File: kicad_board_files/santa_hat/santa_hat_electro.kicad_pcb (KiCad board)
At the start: 2 copper layers, 23.3 x 29.9 mm, 5 parts, among them U1 ELECTRO_HAT

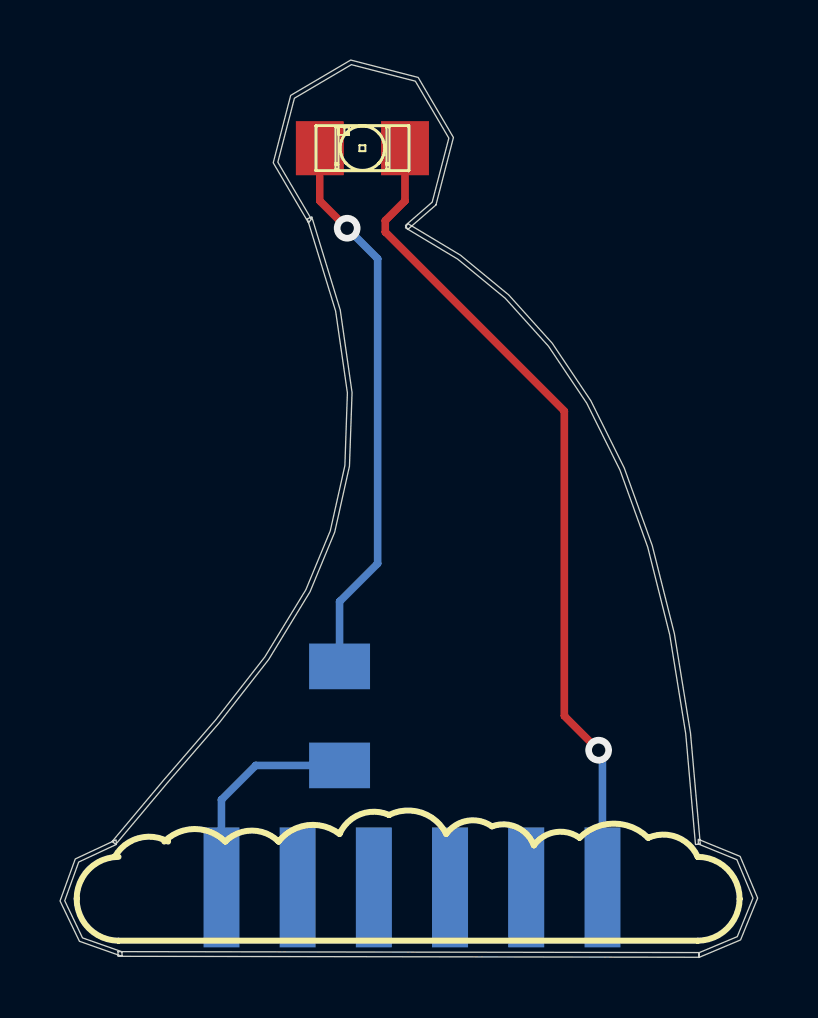
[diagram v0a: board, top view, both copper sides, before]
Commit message: fliped the header to the currect way
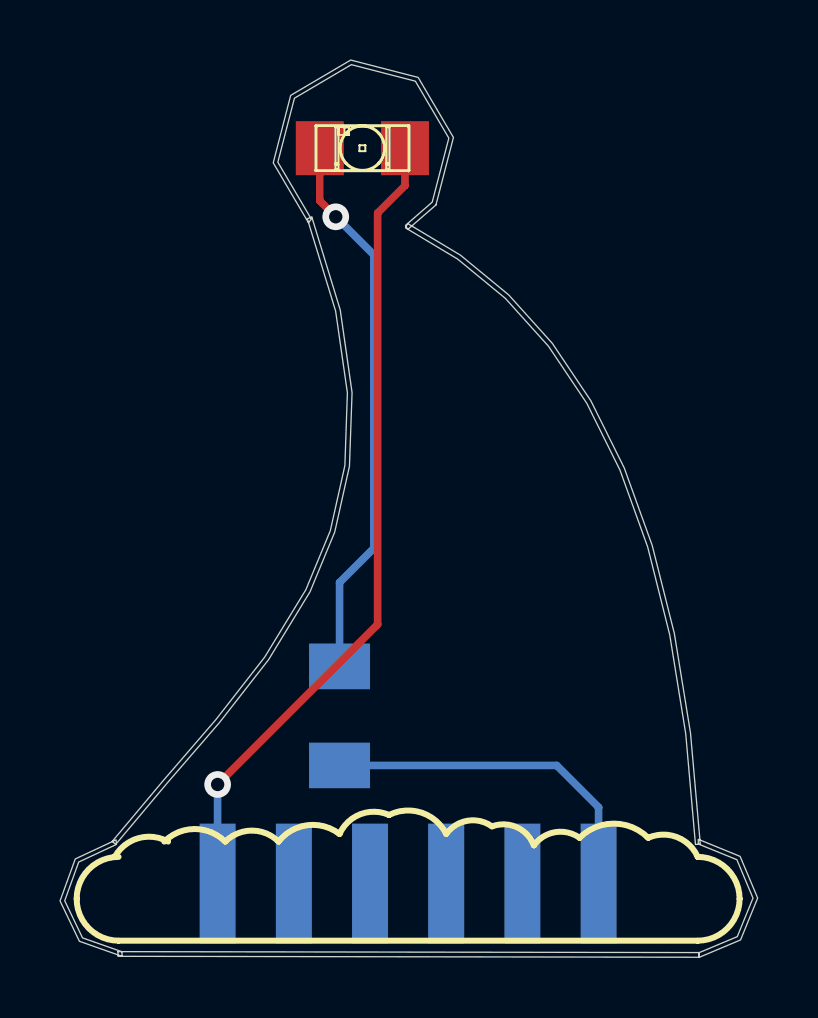
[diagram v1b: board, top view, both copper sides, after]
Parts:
- U1: footprint electro_hat_male_custom -> electro_hat_male_mirrored
- moved U1 0.18 mm to (199.4, 141.6)
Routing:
- net N-000005: track 7.33 -> 11.8 mm
- net N-000007: track 27.9 -> 27.1 mm
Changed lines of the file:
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@@
     (links 3)
     (no_connects 0)
-    (area 187.531625 109.510164 216.1159 148.299836)
+    (area 0 0 0 0)
     (thickness 1.6)
     (drawings 18)
-    (tracks 19)
+    (tracks 16)
     (zones 0)
     (modules 5)
@@
       (scale (xyz 0.17 0.16 0.16))
       (rotate (xyz 0 0 0))
-    )
-  )
-  (module electro_hat_male_custom (layer B.Cu)
-    (at 199.517 141.732)
-    (fp_text reference U1 (at 0 4.445) (layer B.SilkS) hide
-      (effects (font (size 1 1) (thickness 0.15)) (justify mirror))
-    )
-    (fp_text value ELECTRO_HAT (at 0 -4.953) (layer B.SilkS) hide
-      (effects (font (size 1 1) (thickness 0.15)) (justify mirror))
-    )
-    (pad 3 smd rect (at -1.27 0) (size 1.2 4)
-      (layers B.Cu B.Paste B.Mask)
-    )
-    (pad 4 smd rect (at 1.27 0) (size 1.2 4)
-      (layers B.Cu B.Paste B.Mask)
-    )
-    (pad 2 smd rect (at -3.81 0) (size 1.2 4)
-      (layers B.Cu B.Paste B.Mask)
-    )
-    (pad 1 smd rect (at -6.35 0) (size 1.2 4)
-      (layers B.Cu B.Paste B.Mask)
-      (net 1 N-000005)
-    )
-    (pad 5 smd rect (at 3.81 0) (size 1.2 4)
-      (layers B.Cu B.Paste B.Mask)
-    )
-    (pad 6 smd rect (at 6.35 0) (size 1.2 4)
-      (layers B.Cu B.Paste B.Mask)
-      (net 3 N-000007)
     )
   )
@@
       (xy -3.50012 3.50012) (xy -3.50012 3.50012)) (layer B.SilkS) (width 0.00254))
   )
+  (module electro_hat_male_mirrored (layer B.Cu)
+    (at 199.39 141.605)
+    (fp_text reference U1 (at 0 4.445) (layer B.SilkS)
+      (effects (font (size 1 1) (thickness 0.15)) (justify mirror))
+    )
+    (fp_text value ELECTRO_HAT (at 0 -4.953) (layer B.SilkS)
+      (effects (font (size 1 1) (thickness 0.15)) (justify mirror))
+    )
+    (pad 3 smd rect (at 1.27 0) (size 1.2 4)
+      (layers B.Cu B.Paste B.Mask)
+    )
+    (pad 4 smd rect (at -1.27 0) (size 1.2 4)
+      (layers B.Cu B.Paste B.Mask)
+    )
+    (pad 2 smd rect (at 3.81 0) (size 1.2 4)
+      (layers B.Cu B.Paste B.Mask)
+    )
+    (pad 1 smd rect (at 6.35 0) (size 1.2 4)
+      (layers B.Cu B.Paste B.Mask)
+      (net 1 N-000005)
+    )
+    (pad 5 smd rect (at -3.81 0) (size 1.2 4)
+      (layers B.Cu B.Paste B.Mask)
+    )
+    (pad 6 smd rect (at -6.35 0) (size 1.2 4)
+      (layers B.Cu B.Paste B.Mask)
+      (net 3 N-000007)
+    )
+  )
   (gr_text 2016 (at 201.93 128.905) (layer B.SilkS)
     (effects (font (size 1 1) (thickness 0.25)) (justify mirror))
@@
   (gr_arc (start 209.042 142.113) (end 210.439 142.113) (angle 90) (layer F.SilkS) (width 0.2))
   (gr_arc (start 209.042 142.113) (end 209.042 140.716) (angle 90) (layer F.SilkS) (width 0.2))
-  (segment (start 193.167 141.732) (end 193.167 138.811) (width 0.254) (layer B.Cu) (net 1))
-  (segment (start 194.31 137.668) (end 197.104 137.668) (width 0.254) (layer B.Cu) (net 1))
-  (segment (start 193.167 138.811) (end 194.31 137.668) (width 0.254) (layer B.Cu) (net 1))
-  (segment (start 197.104 134.366) (end 197.104 132.207) (width 0.254) (layer B.Cu) (net 2))
-  (segment (start 196.44614 118.84914) (end 196.44614 117.094) (width 0.254) (layer F.Cu) (net 2))
-  (segment (start 197.358 119.761) (end 196.44614 118.84914) (width 0.254) (layer F.Cu) (net 2))
-  (via (at 197.358 119.761) (size 0.889) (layers F.Cu B.Cu) (net 2))
-  (segment (start 198.374 120.777) (end 197.358 119.761) (width 0.254) (layer B.Cu) (net 2))
-  (segment (start 198.374 130.937) (end 198.374 120.777) (width 0.254) (layer B.Cu) (net 2))
-  (segment (start 197.104 132.207) (end 198.374 130.937) (width 0.254) (layer B.Cu) (net 2))
-  (segment (start 199.28586 117.094) (end 199.28586 118.84914) (width 0.254) (layer F.Cu) (net 3))
-  (segment (start 205.867 137.287) (end 205.867 141.732) (width 0.254) (layer B.Cu) (net 3))
-  (segment (start 205.74 137.16) (end 205.867 137.287) (width 0.254) (layer B.Cu) (net 3))
-  (via (at 205.74 137.16) (size 0.889) (layers F.Cu B.Cu) (net 3))
-  (segment (start 204.597 136.017) (end 205.74 137.16) (width 0.254) (layer F.Cu) (net 3))
-  (segment (start 204.597 125.857) (end 204.597 136.017) (width 0.254) (layer F.Cu) (net 3))
-  (segment (start 198.628 119.888) (end 204.597 125.857) (width 0.254) (layer F.Cu) (net 3))
-  (segment (start 198.628 119.507) (end 198.628 119.888) (width 0.254) (layer F.Cu) (net 3))
-  (segment (start 199.28586 118.84914) (end 198.628 119.507) (width 0.254) (layer F.Cu) (net 3))
+  (segment (start 205.74 141.605) (end 205.74 139.065) (width 0.254) (layer B.Cu) (net 1) (status 400000))
+  (segment (start 204.343 137.668) (end 197.104 137.668) (width 0.254) (layer B.Cu) (net 1) (status 800000))
+  (segment (start 205.74 139.065) (end 204.343 137.668) (width 0.254) (layer B.Cu) (net 1))
+  (segment (start 197.104 134.366) (end 197.104 131.572) (width 0.254) (layer B.Cu) (net 2) (status 400000))
+  (segment (start 196.44614 118.84914) (end 196.44614 117.094) (width 0.254) (layer F.Cu) (net 2) (status 800000))
+  (segment (start 196.977 119.38) (end 196.44614 118.84914) (width 0.254) (layer F.Cu) (net 2))
+  (via (at 196.977 119.38) (size 0.889) (layers F.Cu B.Cu) (net 2))
+  (segment (start 198.247 120.65) (end 196.977 119.38) (width 0.254) (layer B.Cu) (net 2))
+  (segment (start 198.247 130.429) (end 198.247 120.65) (width 0.254) (layer B.Cu) (net 2))
+  (segment (start 197.104 131.572) (end 198.247 130.429) (width 0.254) (layer B.Cu) (net 2))
+  (segment (start 199.28586 117.094) (end 199.28586 118.34114) (width 0.254) (layer F.Cu) (net 3) (status 400000))
+  (segment (start 193.04 138.303) (end 193.04 141.605) (width 0.254) (layer B.Cu) (net 3) (status 800000))
+  (via (at 193.04 138.303) (size 0.889) (layers F.Cu B.Cu) (net 3))
+  (segment (start 198.374 132.969) (end 193.04 138.303) (width 0.254) (layer F.Cu) (net 3))
+  (segment (start 198.374 119.253) (end 198.374 132.969) (width 0.254) (layer F.Cu) (net 3))
+  (segment (start 199.28586 118.34114) (end 198.374 119.253) (width 0.254) (layer F.Cu) (net 3))
 )
